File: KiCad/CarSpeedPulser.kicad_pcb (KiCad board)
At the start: 2 copper layers, 43.2 x 66 mm, 17 parts, among them P1 CONN_01X03, P2 CONN_01X05, Q1 2SK4017, SW1 RESET, SW2 UP, SW3 DOWN, U1 LPC810, U2 AE-AQM0802, U3 XC6202P332TB

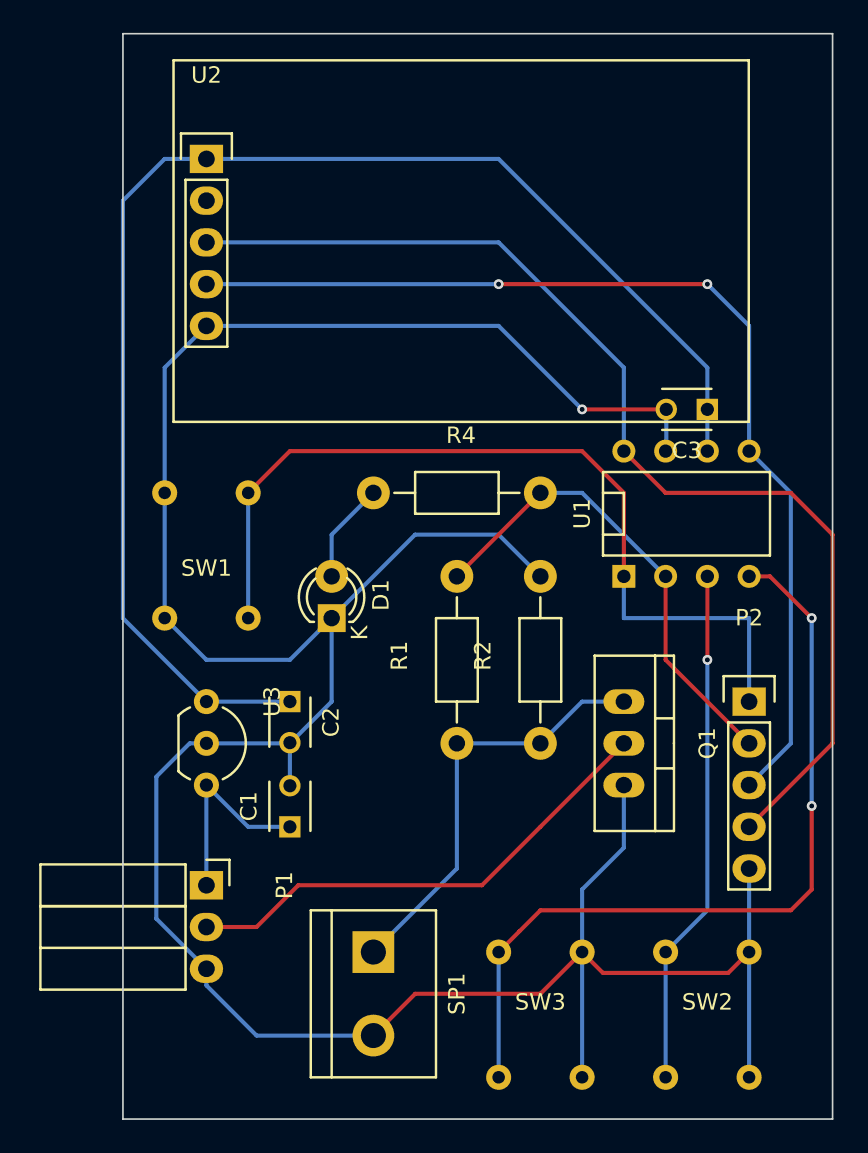
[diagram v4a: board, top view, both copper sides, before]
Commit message: Replaced AE-AQM802 with AQM0802A-RN-GBW.
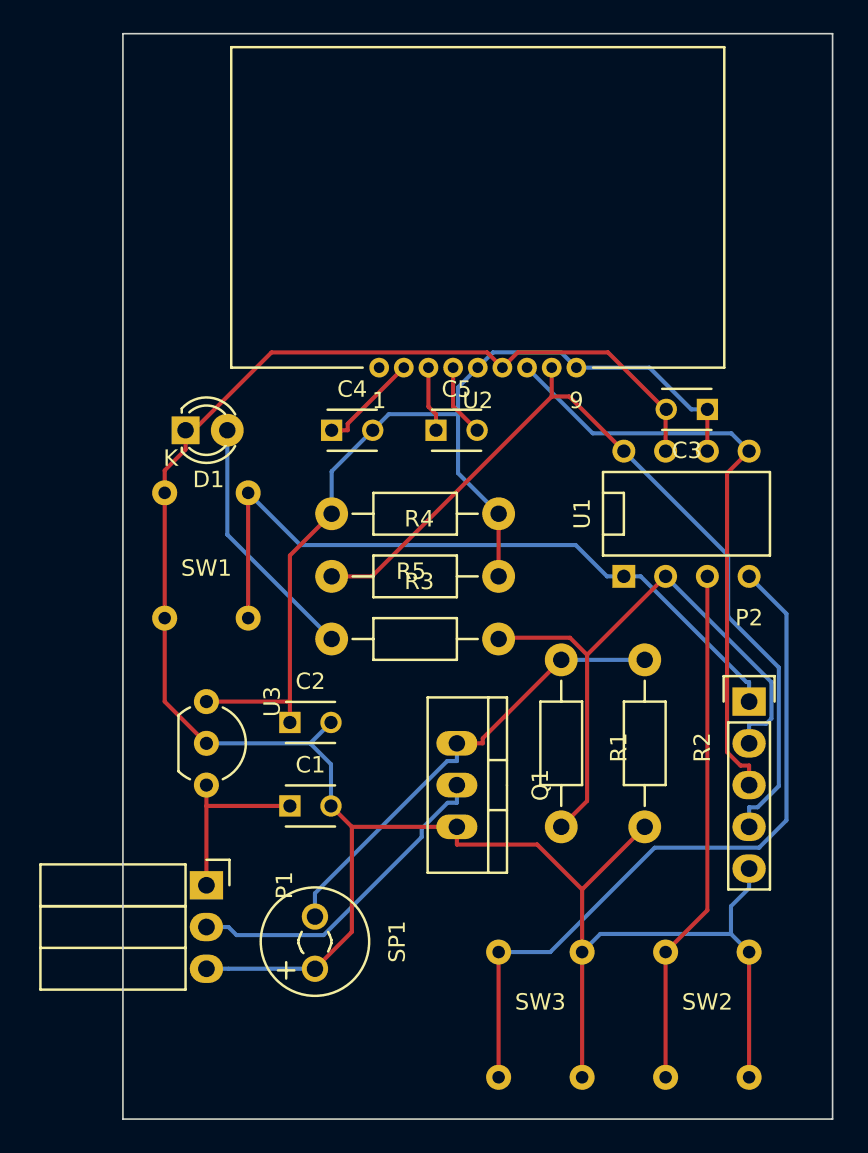
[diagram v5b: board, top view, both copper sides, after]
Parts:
- added C4: 1u, Capacitors_ThroughHole:C_Disc_D3_P2.5, F.Cu at (33.0, 41.9)
- added C5: 1u, Capacitors_ThroughHole:C_Disc_D3_P2.5, F.Cu at (39.4, 41.9)
- added R3: 100, Resistors_ThroughHole:Resistor_Horizontal_RM10mm, F.Cu at (38.1, 54.6)
- added R5: 10k, Resistors_ThroughHole:Resistor_Horizontal_RM10mm, F.Cu at (38.1, 47.0)
- C1: value 0.33u -> 1u
- C2: value 4.7u -> 1u
- R4: value 100 -> 10k
- SP1: footprint Connect:bornier2 -> Buzzers_Beepers:MagneticBuzzer_Kingstate_KCG0601
- U2: value AE-AQM0802 -> AQM0802A-RN-GBW; footprint pulser:AE-AQM0802 -> pulser:AQM0802A-RN-GBW
- moved U2 20.8 mm to (41.9, 38.1)
- moved D1 14.5 mm to (24.1, 41.9), turned to 0 degrees
- moved Q1 10.5 mm to (40.6, 63.5)
- moved R1 8.13 mm to (47.0, 61.0), turned to 270 degrees
- moved R2 8.13 mm to (52.1, 61.0), turned to 270 degrees
- moved SP1 5.89 mm to (32.0, 71.5)
- moved R4 5.68 mm to (38.1, 50.8)
- moved C1 1.27 mm to (30.5, 64.8), turned to 0 degrees
- moved C2 1.27 mm to (30.5, 59.7), turned to 0 degrees
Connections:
- P2 pad 3: Net-(P2-Pad3) -> /SDA
- R4 pad 1: Net-(D1-Pad2) -> Net-(P2-Pad4)
- R4 pad 2: Net-(P2-Pad2) -> VDD
- U1 pad 5: Net-(P2-Pad3) -> /SDA
- U2 pad 1: VDD -> Net-(U2-Pad1)
- U2 pad 3: Net-(P2-Pad4) -> Net-(C5-Pad1)
- U2 pad 4: Net-(P2-Pad3) -> Net-(C5-Pad2)
- U2 pad 5: GND -> VDD
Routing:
- net Net-(P2-Pad3): track 64.1 -> 0.00 mm, vias 2 -> 0
- net GND: track 182.8 -> 143.4 mm, vias 1 -> 0
- net /SDA: track 0.00 -> 37.4 mm
- net VDD: track 84.6 -> 63.1 mm
- net Net-(P2-Pad4): track 68.3 -> 53.3 mm
- net /PULSE: track 30.0 -> 20.2 mm
- net Net-(D1-Pad2): track 6.13 -> 15.3 mm
- net Net-(P2-Pad1): track 52.9 -> 44.1 mm
- net Net-(P2-Pad2): track 29.2 -> 37.7 mm
- net Net-(C4-Pad1): track 0.00 -> 6.20 mm
- net Net-(SW3-Pad1): track 49.6 -> 44.2 mm, vias 2 -> 0
- net Net-(C5-Pad2): track 0.00 -> 4.41 mm
- net Net-(C5-Pad1): track 0.00 -> 4.00 mm
- net Net-(Q1-Pad1): track 26.0 -> 28.2 mm
- net +12V: track 12.2 -> 11.2 mm
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
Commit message: Added a footprint of terminal block.
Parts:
- P1: footprint Socket_Strips:Socket_Strip_Angled_1x03 -> pulser:TB401-1-3-E
- Q1: footprint Transistors_TO-220:TO-220_Neutral123_Vertical -> Transistors_TO-220:TO-220_FET-GDS_Vertical
- moved P1 8.21 mm to (28.4, 77.2), turned to 90 degrees
- moved SP1 4.91 mm to (36.8, 72.4)
- moved SW1 4.02 mm to (26.7, 49.5), turned to 270 degrees
- moved SW2 4.02 mm to (54.6, 77.5), turned to 270 degrees
- moved SW3 3.81 mm to (43.2, 77.5), turned to 270 degrees
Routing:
- net (no net): track 0.00 -> 64.1 mm
- net /PULSE: track 20.2 -> 0.00 mm
- net Net-(Q1-Pad1): track 28.2 -> 13.7 mm
- net GND: track 143.4 -> 129.1 mm
- net Net-(SW3-Pad1): track 44.2 -> 36.6 mm
- net Net-(P2-Pad1): track 44.1 -> 36.4 mm
